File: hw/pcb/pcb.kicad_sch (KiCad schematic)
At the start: 9 parts, among them U1 ICL3232, U2 74AHC240, U3 MAX3232, U4 74AHC240, U5 74AHC273, U6 PI6C5946002ZH, U7 PI6C5946002ZH

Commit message: w5500-evb-pico footprint
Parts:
- removed R1: R_Small, symbol Device:R_Small
- removed U1: ICL3232, symbol Interface_UART:ICL3232
- removed U2, U4: 74AHC240, symbol 74xx:74AHC240
- removed U5: 74AHC273, symbol 74xx:74AHC273
- removed U6, U7: PI6C5946002ZH, Package_DFN_QFN:TQFN-16-1EP_3x3mm_P0.5mm_EP1.6x1.6mm, symbol Buffer:PI6C5946002ZH
- removed W5500-EVB-Pico1: ~, symbol RaspberryPi-Pico:W5500-EVB-Pico
- added W5500-EVB-Pico1: ~, symbol w5500-evb-pico:W5500-EVB-Pico

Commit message: kicad data & hw parts info
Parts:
- added C1: 10uF, Capacitor_SMD:C_1210_3225Metric, symbol Device:C
- added C2: 0.1uF, Capacitor_SMD:C_0805_2012Metric, symbol Device:C
- added C3: 220pF, Capacitor_SMD:C_0805_2012Metric, symbol Device:C
- added C4: 22uF, Capacitor_SMD:C_1210_3225Metric, symbol Device:C
- added D1: SS34, 0.winners:DIOM7959X265N_SS34, symbol SS34:SS34
- added L1: RLF7030T-4R7M3R4, 0.winners:INDP7368X320_Inductor, symbol RLF7030T-4R7M3R4:RLF7030T-4R7M3R4
- added R1: 100K, Resistor_SMD:R_0805_2012Metric, symbol Device:R_US
- added R2: 24K9, Resistor_SMD:R_0805_2012Metric, symbol Device:R_US
- added R3: 200K, Resistor_SMD:R_0805_2012Metric, symbol Device:R_US
- added R4: 68K, Resistor_SMD:R_0805_2012Metric, symbol Device:R_US
- added R5: 124K, Resistor_SMD:R_0805_2012Metric, symbol Device:R_US
- added R6: 40K2, Resistor_SMD:R_0805_2012Metric, symbol Device:R_US
- added U1: MP1584EN, 0.winners:SOIC127P600X170-9N_MP1584EN, symbol MP1584EN:MP1584EN
- W5500-EVB-Pico1: footprint (none) -> 0.winners:W5500-EVB-Pico_SMT_THT
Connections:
- new net: R5.2, R6.1, U1.4 (FB)
- new net: C2.2, D1.C, L1.1, U1.1 (SW)
- new net: R1.2, R2.1, U1.2 (EN)
- new net: C3.1, U1.3 (COMP)
- new net: R3.1, U1.6 (FREQ)
- new net: C2.1, U1.8 (BST)
- new net: C4.1, L1.2, R5.1
- new net: C3.2, R4.1
- new net +24V: C1.1, R1.1, U1.7 (VIN)
- new net GND: C1.2, C4.2, D1.A, R2.2, R3.2, R4.2, R6.2, U1.5 (GND), U1.9 (GND)
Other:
- moved on the sheet: U3, W5500-EVB-Pico1

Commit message: kicad sch
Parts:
- added RaspberryPi-Pico-W1: RaspberryPi Pico W, symbol pico-w:RaspberryPi Pico W
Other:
- moved on the sheet: U3
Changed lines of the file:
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@@
     )
   )
-  (symbol (lib_id "Interface_UART:MAX3232") (at 191.77 116.84 0) (unit 1)
-    (in_bom yes) (on_board yes) (dnp no) (fields_autoplaced)
-    (property "Reference" "U3" (at 193.7259 88.4301 0)
-      (effects (font (size 1.27 1.27)) (justify left))
-    )
-    (property "Value" "MAX3232" (at 193.7259 90.3511 0)
-      (effects (font (size 1.27 1.27)) (justify left))
-    )
-    (property "Footprint" "" (at 193.04 143.51 0)
+  (symbol (lib_id "Interface_UART:MAX3232") (at 251.46 115.57 0) (unit 1)
+    (in_bom yes) (on_board yes) (dnp no) (fields_autoplaced)
+    (property "Reference" "U3" (at 253.4159 87.1601 0)
+      (effects (font (size 1.27 1.27)) (justify left))
+    )
+    (property "Value" "MAX3232" (at 253.4159 89.0811 0)
+      (effects (font (size 1.27 1.27)) (justify left))
+    )
+    (property "Footprint" "" (at 252.73 142.24 0)
       (effects (font (size 1.27 1.27)) (justify left) hide)
     )
-    (property "Datasheet" "https://datasheets.maximintegrated.com/en/ds/MAX3222-MAX3241.pdf" (at 191.77 114.3 0)
+    (property "Datasheet" "https://datasheets.maximintegrated.com/en/ds/MAX3222-MAX3241.pdf" (at 251.46 113.03 0)
       (effects (font (size 1.27 1.27)) hide)
     )
@@
     )
   )
+  (symbol (lib_id "pico-w:RaspberryPi Pico W") (at 165.1 114.3 0) (unit 1)
+    (in_bom yes) (on_board yes) (dnp no) (fields_autoplaced)
+    (property "Reference" "RaspberryPi-Pico-W1" (at 165.1 85.3981 0)
+      (effects (font (size 1.27 1.27)))
+    )
+    (property "Value" "RaspberryPi Pico W" (at 166.37 144.78 0)
+      (effects (font (size 1.27 1.27)) hide)
+    )
+    (property "Footprint" "" (at 165.1 149.86 0)
+      (effects (font (size 1.27 1.27)) hide)
+    )
+    (property "Datasheet" "" (at 165.1 149.86 0)
+      (effects (font (size 1.27 1.27)) hide)
+    )
+    (pin "1")
+    (pin "20")
+    (pin "23")
+    (pin "39")
+    (pin "40")
+    (pin "10")
+    (pin "11")
+    (pin "12")
+    (pin "13")
+    (pin "14")
+    (pin "15")
+    (pin "16")
+    (pin "17")
+    (pin "18")
+    (pin "19")
+    (pin "2")
+    (pin "21")
+    (pin "22")
+    (pin "24")
+    (pin "25")
+    (pin "26")
+    (pin "27")
+    (pin "28")
+    (pin "29")
+    (pin "3")
+    (pin "30")
+    (pin "31")
+    (pin "32")
+    (pin "33")
+    (pin "34")
+    (pin "35")
+    (pin "36")
+    (pin "37")
+    (pin "38")
+    (pin "4")
+    (pin "5")
+    (pin "6")
+    (pin "7")
+    (pin "8")
+    (pin "9")
+    (instances
+      (project "pcb"
+        (path "/9c82e7ff-6b3b-47c7-b218-2bfb4c637bee"
+          (reference "RaspberryPi-Pico-W1") (unit 1)
+        )
+      )
+    )
+  )
   (symbol (lib_id "power:GND") (at 53.34 41.91 0) (unit 1)
     (in_bom yes) (on_board yes) (dnp no) (fields_autoplaced)
@@
   )
   (symbol (lib_id "w5500-evb-pico:W5500-EVB-Pico") (at 93.98 114.3 0) (unit 1)
-    (in_bom yes) (on_board yes) (dnp no) (fields_autoplaced)
-    (property "Reference" "W5500-EVB-Pico1" (at 93.98 143.8355 0)
-      (effects (font (size 1.27 1.27)))
-    )
+    (in_bom yes) (on_board yes) (dnp no)
+    (property "Reference" "W5500-EVB-Pico1" (at 93.98 135.89 0)
+      (effects (font (size 1.27 1.27)))
+    )

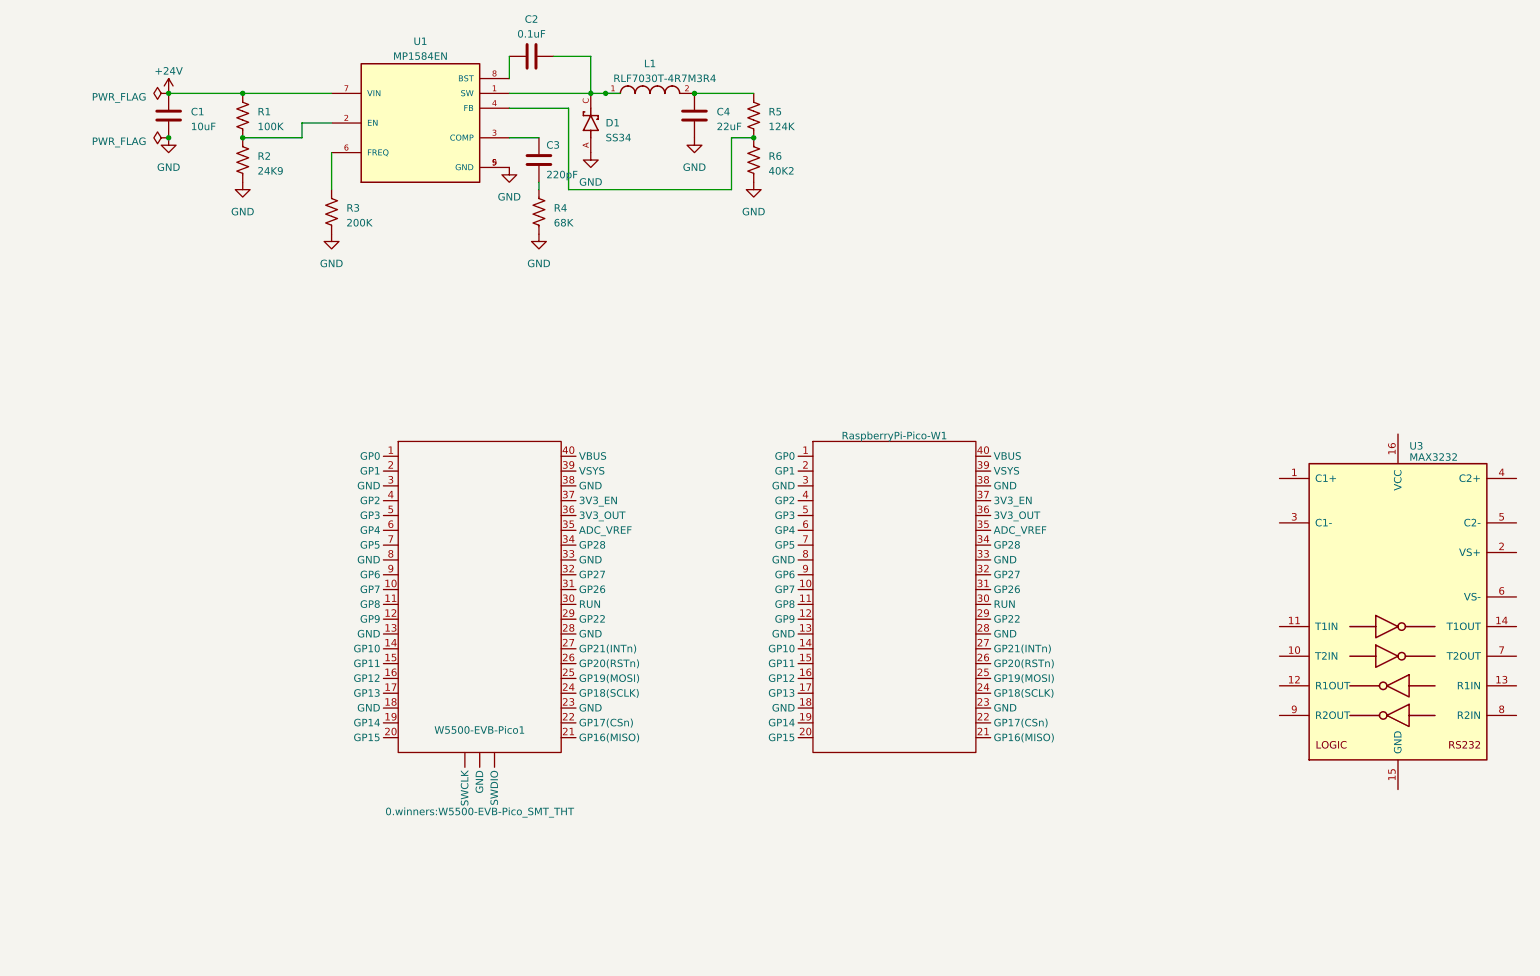
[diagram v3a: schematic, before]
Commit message: schematic v1 completed
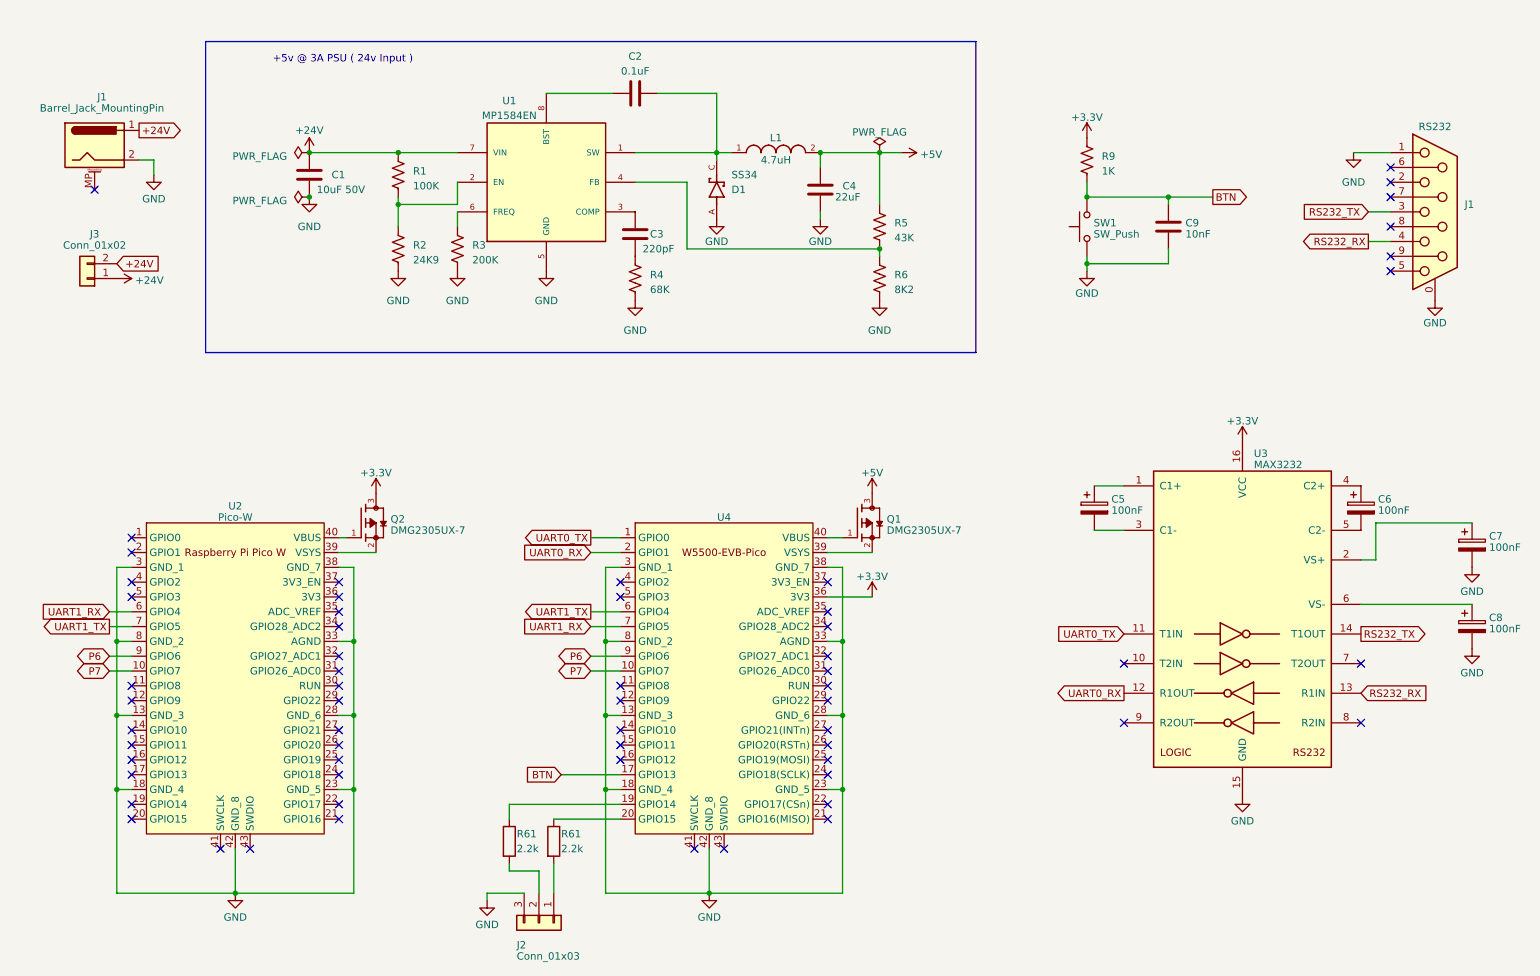
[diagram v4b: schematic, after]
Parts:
- removed RaspberryPi-Pico-W1: RaspberryPi Pico W, symbol pico-w:RaspberryPi Pico W
- removed W5500-EVB-Pico1: ~, 0.winners:W5500-EVB-Pico_SMT_THT, symbol w5500-evb-pico:W5500-EVB-Pico
- added C5, C6, C7, C8: 100nF, Capacitor_SMD:C_0402_1005Metric, symbol Device:C_Polarized
- added C9: 10nF, symbol Device:C
- added J1: RS232, Connector_Dsub:DSUB-9_Male_Horizontal_P2.77x2.84mm_EdgePinOffset7.70mm_Housed_MountingHolesOffset9.12mm, symbol Connector:DE9_Receptacle_MountingHoles
- added J1: Barrel_Jack_MountingPin, symbol Connector:Barrel_Jack_MountingPin
- added J2: Conn_01x03, symbol Connector_Generic:Conn_01x03
- added J3: Conn_01x02, symbol Connector_Generic:Conn_01x02
- added Q1, Q2: DMG2305UX-7, SOT91P240X110-3N_DMG2305UX-7, symbol dmg2305-FET:DMG2305UX-7
- added R61 (x2): 2.2k, Resistor_SMD:R_0603_1608Metric, symbol Device:R
- added R9: 1K, Resistor_SMD:R_0805_2012Metric, symbol Device:R_US
- added SW1: SW_Push, symbol Switch:SW_Push
- added U2: Pico-W, MCU_RaspberryPi_and_Boards:RPi_Pico_SMD_TH, symbol raspberrypi-pico-w:Pico-W
- added U4: ~, symbol w5500-evb-pico:W5500-EVB-Pico
- C1: value 10uF -> 10uF 50V
- D1: symbol SS34:SS34 -> ss34:SS34
- L1: value RLF7030T-4R7M3R4 -> 4.7uH; symbol RLF7030T-4R7M3R4:RLF7030T-4R7M3R4 -> rlf7030t-4r7m3r4:RLF7030T-4R7M3R4; MANUFACTURER TDK -> (none); Manufacturer (none) -> TDK; Name (none) -> RLF7030T-4R7M3R4
- R5: value 124K -> 43K
- R6: value 40K2 -> 8K2
- U1: symbol MP1584EN:MP1584EN -> mp1584en:MP1584EN
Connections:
- net +24V: now also J1.1, J3.1 (Pin_1), J3.2 (Pin_2)
- net GND: now also U3.15 (GND), C7.2, C8.2, C9.2, J1.0 (PAD), J1.1, J1.2, J2.3 (Pin_3), SW1.1, U2.13 (GND_3), U2.18 (GND_4), U2.23 (GND_5), U2.28 (GND_6), U2.3 (GND_1), U2.33 (AGND), U2.38 (GND_7), U2.42 (GND_8), U2.8 (GND_2), U4.13 (GND_3), U4.18 (GND_4), U4.23 (GND_5), U4.28 (GND_6), U4.3 (GND_1), U4.33 (AGND), U4.38 (GND_7), U4.42 (GND_8), U4.8 (GND_2); no longer U1.9 (GND)
- net +5V: now reaches C4.1, L1.2, R5.1
- net +5V: now also Q1.3
- net at U3.1 (C1+): now also C5.1
- net UART0_TX: now reaches U3.11 (T1IN)
- net UART0_TX: now also U4.1 (GPIO0)
- net UART0_RX: now reaches U3.12 (R1OUT)
- net UART0_RX: now also U4.2 (GPIO1)
- net RS232_RX: now reaches U3.13 (R1IN)
- net RS232_RX: now also J1.4
- net RS232_TX: now reaches U3.14 (T1OUT)
- net RS232_TX: now also J1.3
- net +3.3V: now reaches U3.16 (VCC)
- net +3.3V: now also Q2.3, R9.1, U4.36 (3V3)
- net at U3.2 (VS+): now also C7.1
- net at U3.3 (C1-): now also C5.2
- net at U3.4 (C2+): now also C6.1
- net at U3.5 (C2-): now also C6.2
- net at U3.6 (VS-): now also C8.1
- new net: J2.1 (Pin_1), R61.2
- new net: J2.2 (Pin_2), R61.2
- new net: R61.1, U4.19 (GPIO14)
- new net: R61.1, U4.20 (GPIO15)
- new net: Q1.2, U4.39 (VSYS)
- new net: Q1.1, U4.40 (VBUS)
- new net: Q2.1, U2.40 (VBUS)
- new net: Q2.2, U2.39 (VSYS)
- new net BTN: C9.1, R9.2, SW1.2, U4.17 (GPIO13)
- new net P6: U2.9 (GPIO6), U4.9 (GPIO6)
- new net P7: U2.10 (GPIO7), U4.10 (GPIO7)
- new net UART1_RX: U2.6 (GPIO4), U4.7 (GPIO5)
- new net UART1_TX: U2.7 (GPIO5), U4.6 (GPIO4)
- no-connect marks 0 -> 61
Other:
- note added: "+5v @ 3A PSU ( 24v Input )"
- moved on the sheet: C1, C2, C3, C4, D1, L1, R1, R2, R3, R4, R5, R6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
